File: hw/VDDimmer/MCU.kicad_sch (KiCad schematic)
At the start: 24 parts, among them J1 USB-C 16P, J11 BTN1, J12 BTN2, J13 EXP 3V3/GND/SDA/SCL/EN/IO0, J14 UART1 3V3/GND/TX/RX, U1 ESP32-S3-WROOM-1-N16R8

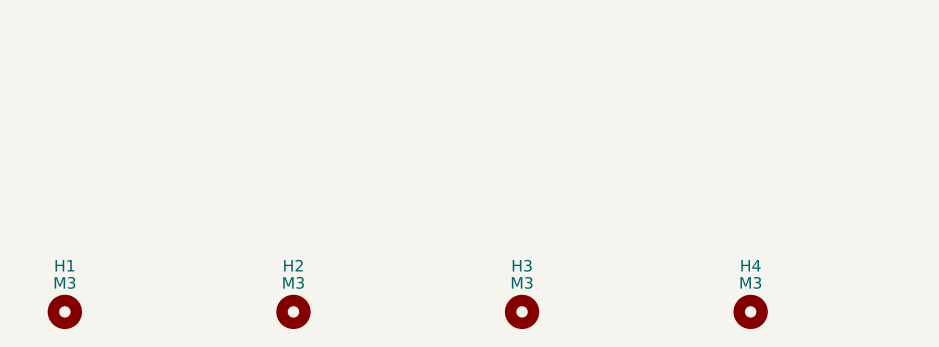
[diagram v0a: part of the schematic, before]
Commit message: Place power entry and conversion on the left edge
Rev A put power in at the north edge and outputs at the south, forcing the
~5 A VIN_PROT rail across the board through the MCU/USB region. This inverts
that: J2 sits on the left edge at (109.5, 106) rot 270 with its opening facing
the edge, and F1 -> D5 -> Q5 (Q_REV) run directly inboard of it at y 106, so
the full input current never leaves the bottom-left corner.

The buck cluster was translated RIGIDLY by (-56, +6) rather than re-placed
part by part. Rev A's Cin hot loop measured 2.51 mm2 against a 15 mm2 gate;
moving U2, C20-C24, L1, C25/C26 and the R21/R22/C27 divider as one block
preserves that geometry by construction instead of gambling on re-derivation.
measure.py confirms: loop area 2.51 mm2, 0 vias inside the loop bbox.

Connector orientation was measured, not assumed: all four connector families
on this board (JST XH 2- and 4-way, Phoenix MC, USB-C) face +y at rotation 0,
so J2 needs rot 270 to open onto the left edge.

H3 and H4 move up to y 118.5, out of the harness band. Their 5.90 mm keepouts
at y 135.5 sat exactly where J3 and J1 need to be - a collision the plan does
not anticipate. At 118.5 H4 genuinely separates J2 (courtyard bottom 114.18)
from J3 (courtyard top 126.64), which is the job spec section 5.1 gives it.

measure.py sections 2-4 still report against Rev A's stale copper (SW segments
at the old x 177-179 buck location), so those clearances are meaningless until
Phase 5 re-routes. Section 1 is the gate, and it passes.

Co-Authored-By: Claude Opus 5 (1M context) <noreply@anthropic.com>
Claude-Session: https://claude.ai/code/session_01YZHVU8aymL4RkLeCfwomwj
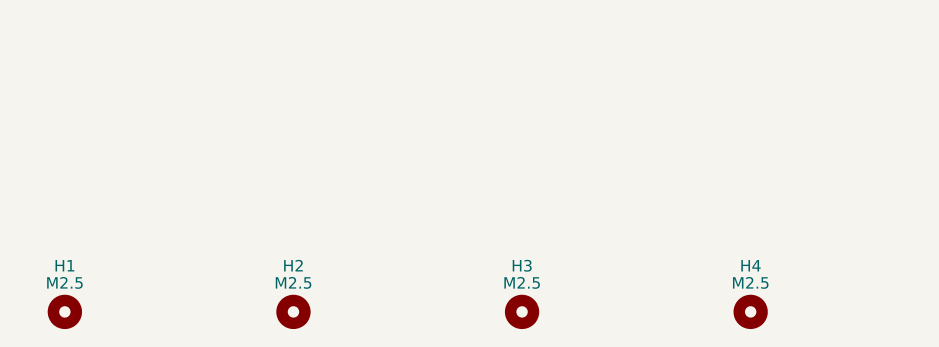
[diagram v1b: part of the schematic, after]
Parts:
- H1, H2, H3, H4: value M3 -> M2.5
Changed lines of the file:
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@@
 			)
 		)
-		(property "Value" "M3"
+		(property "Value" "M2.5"
 			(at 90.17 247.015 0)
 			(show_name no)
@@
 			)
 		)
-		(property "Value" "M3"
+		(property "Value" "M2.5"
 			(at 64.77 247.015 0)
 			(show_name no)
@@
 			)
 		)
-		(property "Value" "M3"
+		(property "Value" "M2.5"
 			(at 39.37 247.015 0)
 			(show_name no)
@@
 			)
 		)
-		(property "Value" "M3"
+		(property "Value" "M2.5"
 			(at 115.57 247.015 0)
 			(show_name no)
